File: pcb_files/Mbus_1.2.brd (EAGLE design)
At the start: 98.7 x 71.1 mm, 50 parts, among them IC1 NCP1117ST50T3G, IC3 ATMEGA2560-16AU, IC4 RTC_PCF8523T, J1 F-1X18-SIP-100-32Y, J2 USB_A_SMT_FEMALE, M1 SERVO, Q2 32.768, Y1 CSTCE16M0V53-R0 16MHZ

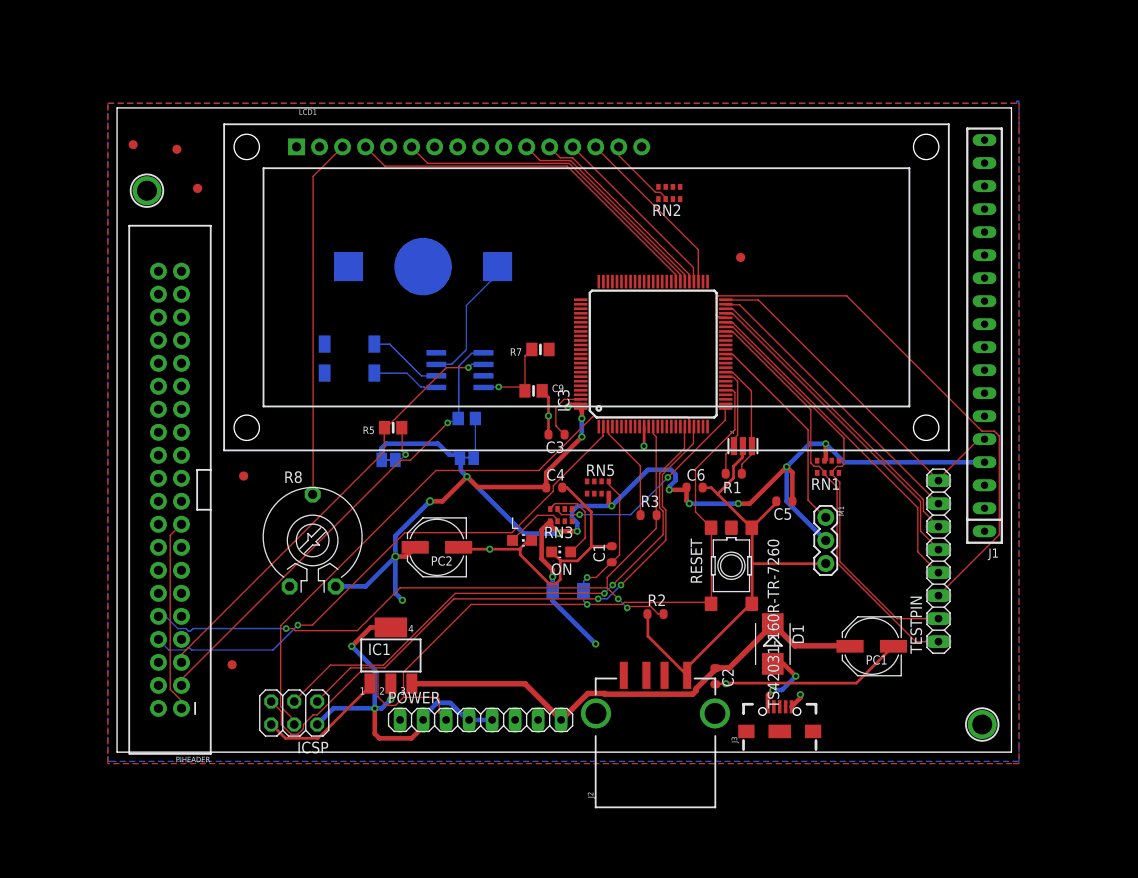
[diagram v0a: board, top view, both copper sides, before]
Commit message: Add the voltage level shifter circuit for uart in version 1.2.
Signed-off-by: Yiteng Cai <alonsochate@umich.edu>
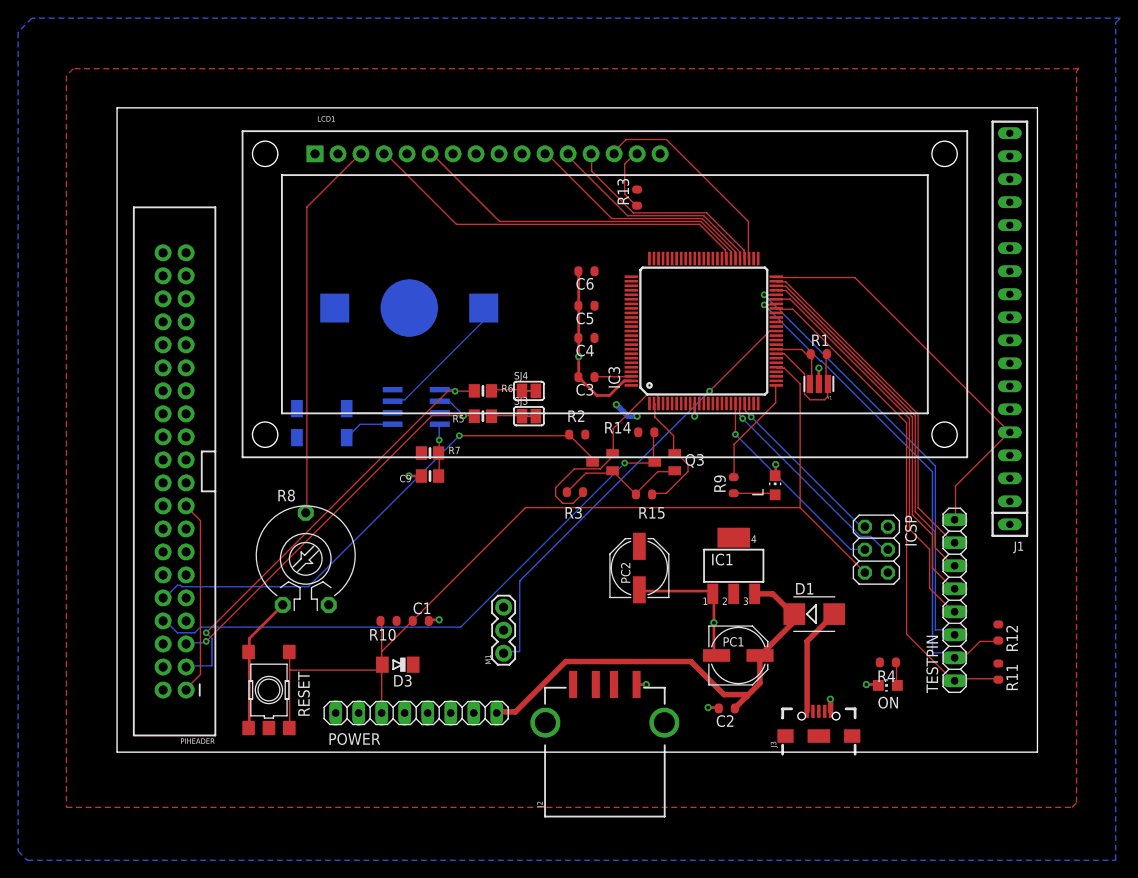
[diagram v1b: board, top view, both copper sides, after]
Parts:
- removed FD1, FD2, FD3, FD4: FIDUCIALMOUNT, SmartPrj:FIDUCIA-MOUNT
- removed FID3, FID4: FIDUCIAL"", microbuilder:FIDUCIAL_1MM
- removed RN1, RN5: 10K, resistor-dil:CAT16
- removed RN2: 220, resistor-dil:CAY16
- removed RN3: 1k, resistor-dil:CAY16
- removed U$2, U$3: MOUNTINGHOLE2.0, microbuilder:MOUNTINGHOLE_2.0_PLATED
- added Q1, Q3: BSS138, adafruit:SOT23
- added R10, R11, R12, R14, R15: 10k, SmartPrj:R0603-ROUND
- added R13: 220, SmartPrj:R0603-ROUND
- added R4, R9: 1k, SmartPrj:R0603-ROUND
- R2: value 3.3k -> 10k
- R3: value 1.6k -> 10k
- R8: device rcl:PT-10 -> rcl@1:PT-10
- moved ICSP 66.7 mm to (83.8, 22.4), turned to 270 degrees
- moved RESET 52.9 mm to (16.8, 6.86), turned to 90 degrees
- moved IC1 39.1 mm to (68.1, 20.6)
- moved ON 39.0 mm to (85.1, 7.37)
- moved M1 38.6 mm to (42.7, 10.9), turned to 90 degrees
- moved C5 30.7 mm to (51.8, 49.3)
- moved L 28.6 mm to (72.6, 29.5), turned to 0 degrees
- moved C6 26.7 mm to (51.8, 53.1), turned to 180 degrees
- moved PC2 22.5 mm to (57.7, 20.3), turned to 90 degrees
- moved C1 22.3 mm to (33.5, 14.5), turned to 0 degrees
- moved R2 21.6 mm to (50.8, 35.1)
- moved D3 20.5 mm to (31.0, 9.65), flipped to the top
- moved C4 16.9 mm to (51.8, 45.7), turned to 180 degrees
- moved R7 16.7 mm to (34.5, 33.0), turned to 0 degrees
- moved SJ3 16.2 mm to (45.5, 37.1), flipped to the top
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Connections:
- new net +3V3: Q1.1, Q3.1, R15.2, R3.2
- new net N$1: PIHEADER.10, Q1.3, R2.1
- new net N$12: PIHEADER.8, Q3.3, R14.1
- net +5V: now also R10.1, R11.1, R12.1, R13.2, R14.2, R2.2, R4.2; no longer RN1.6, RN1.7, RN2.7, RN3.1, RN5.8
- net GND: no longer R2.1
- net N$11: now also R13.1; no longer RN2.2
- net N$2: now also R9.1; no longer RN3.2
- net N$3: now also R4.1; no longer RN3.8
- net PB7: now also R9.2; no longer RN3.7
- net RESET: now also R10.2; no longer RN5.1
- net RXD0: now also Q3.2, R15.1; no longer PIHEADER.8
- net SCL: now also R11.2; no longer RN1.2
- net SDA: now also R12.2; no longer RN1.3
- net TXD0: now also Q1.2
- net TXD2: no longer PIHEADER.10, R2.2, R3.2
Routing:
- net +5V: track 213.0 -> 2.81 mm, vias 19 -> 2
- net TXD2: track 80.2 -> 0.00 mm, vias 3 -> 0
- net GND: track 133.4 -> 61.8 mm, vias 6 -> 11
- net N$12: track 0.00 -> 66.1 mm, vias 0 -> 1
- net N$1: track 0.00 -> 56.7 mm, vias 0 -> 1
- net RXD0: track 61.0 -> 14.4 mm, vias 1 -> 0
- net PB2: track 67.1 -> 23.8 mm, vias 0 -> 1
- net PB3: track 60.0 -> 19.4 mm, vias 2 -> 1
- net PB1: track 61.6 -> 23.0 mm, vias 2 -> 1
- net PL3: track 23.1 -> 49.4 mm, vias 0 -> 1
- net +3V3: track 0.00 -> 15.1 mm
- net TXD1: track 61.2 -> 48.5 mm, vias 0 -> 1
- net PB7: track 24.5 -> 12.1 mm, vias 2 -> 0
- net TXD0: track 11.3 -> 23.2 mm
- net SDA: track 47.0 -> 55.9 mm, vias 0 -> 1
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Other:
- board size 98.7 x 71.1 mm -> 101.6 x 71.1 mm
